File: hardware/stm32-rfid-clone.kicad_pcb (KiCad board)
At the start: 2 copper layers, 61 x 61 mm, 112 parts, among them J101 USB, M101 Mouting Hole, M102 Mouting Hole, M103 Mouting Hole, M104 Mouting Hole, P101 JTAG10, P102 BATTERY, P103 DEBUG, P104 READIND, P105 SPEAKER, P201 ANT, Q201 2N2222, Q202 2N2222, Q203 2N2907, U101 MOSFET-P, U102 STM32-48PIN, U103 AP6502, U104 MOSFET-N, U105 MIC2288, U201 TL084, X101 8MHz, X102 32.768kHz

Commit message: moved labels
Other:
- board text added: "+"
- board text added: "-"
- board text added: "ANT"
- board text added: "BAT"
- board text added: "DEBUG"
- board text added: "GND"
- board text added: "GRN"
- board text added: "JTAG"
- board text added: "LED"
- board text added: "PWR"
- board text added: "RED"
- board text added: "RF1"
- board text added: "RF2"
- board text added: "RF3"
- board text added: "RF4"
- board text added: "RX"
- board text added: "SPK"
- board text added: "THRESHOLD"
- board text added: "TX"
- board text added: "WRITEEN"

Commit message: update values
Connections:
- R115 pad 1: +3.3V -> +9V
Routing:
- net +3.3V: track 217.4 -> 201.4 mm
- net +9V: track 54.2 -> 62.3 mm, vias 2 -> 4
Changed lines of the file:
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@@
     (links 208)
     (no_connects 0)
-    (area 80.4478 75.353519 142.290001 148.628201)
+    (area 81.229999 78.689999 142.290001 139.750001)
     (thickness 1.6)
     (drawings 29)
-    (tracks 815)
+    (tracks 816)
     (zones 0)
     (modules 112)
@@
       (outputformat 1)
       (mirror false)
-      (drillshape 1)
+      (drillshape 0)
       (scaleselection 1)
       (outputdirectory ""))
@@
     (fp_line (start -1.7 1) (end -1.7 -1) (layer Cmts.User) (width 0.1))
     (pad 1 smd rect (at -0.95 0 270) (size 1 1.45) (layers F.Cu F.Paste F.Mask)
-      (net 1 +3.3V))
+      (net 2 +9V))
     (pad 2 smd rect (at 0.95 0 270) (size 1 1.45) (layers F.Cu F.Paste F.Mask)
       (net 50 "Net-(D105-Pad2)"))
@@
   (segment (start 87.2 102) (end 87.2 104.3) (width 0.254) (layer F.Cu) (net 1))
   (segment (start 85.96 100.76) (end 87.2 102) (width 0.254) (layer F.Cu) (net 1))
-  (segment (start 118 89.05) (end 118.55 89.05) (width 0.254) (layer F.Cu) (net 1))
-  (segment (start 118.55 89.05) (end 119.4 89.9) (width 0.254) (layer F.Cu) (net 1))
-  (segment (start 119.4 89.9) (end 119.4 91.7) (width 0.254) (layer F.Cu) (net 1))
-  (segment (start 119.4 91.7) (end 118.6 92.5) (width 0.254) (layer F.Cu) (net 1))
-  (segment (start 118.6 92.5) (end 115.7 92.5) (width 0.254) (layer F.Cu) (net 1))
-  (segment (start 115.7 92.5) (end 110 98.2) (width 0.254) (layer F.Cu) (net 1))
-  (segment (start 110 98.2) (end 110 98.55) (width 0.254) (layer F.Cu) (net 1))
   (segment (start 98.75 97.75) (end 98.75 96.65) (width 0.254) (layer F.Cu) (net 1))
   (segment (start 98.75 96.65) (end 97.55 95.45) (width 0.254) (layer F.Cu) (net 1))
@@
   (segment (start 115 126.45) (end 112.1 126.45) (width 0.4) (layer F.Cu) (net 1))
   (segment (start 112.1 126.45) (end 112 126.55) (width 0.4) (layer F.Cu) (net 1))
+  (segment (start 122.05 94.5) (end 122.05 94.05) (width 0.4) (layer F.Cu) (net 2))
+  (segment (start 118.55 89.05) (end 118 89.05) (width 0.4) (layer F.Cu) (net 2))
+  (segment (start 120.8 91.3) (end 118.55 89.05) (width 0.4) (layer F.Cu) (net 2))
+  (via (at 120.8 91.3) (size 0.889) (layers F.Cu B.Cu) (net 2))
+  (segment (start 122.8 93.3) (end 120.8 91.3) (width 0.4) (layer B.Cu) (net 2))
+  (via (at 122.8 93.3) (size 0.889) (layers F.Cu B.Cu) (net 2))
+  (segment (start 122.05 94.05) (end 122.8 93.3) (width 0.4) (layer F.Cu) (net 2))
   (segment (start 130.3 107.1) (end 129.4 106.2) (width 0.4) (layer B.Cu) (net 2))
   (via (at 124.1 100) (size 0.889) (layers F.Cu B.Cu) (net 2))
@@
   (segment (start 114.5 120.55) (end 112.95 120.55) (width 0.254) (layer F.Cu) (net 48))
   (segment (start 112.95 120.55) (end 112 119.6) (width 0.254) (layer F.Cu) (net 48))
-  (segment (start 114.3 81.28) (end 114.3 85.35) (width 0.254) (layer F.Cu) (net 49))
-  (segment (start 114.3 85.35) (end 114.45 85.5) (width 0.254) (layer F.Cu) (net 49))
-  (segment (start 115.15 90) (end 115.15 89.05) (width 0.254) (layer F.Cu) (net 49))
-  (segment (start 114.45 88.35) (end 114.45 85.5) (width 0.254) (layer F.Cu) (net 49))
-  (segment (start 115.15 89.05) (end 114.45 88.35) (width 0.254) (layer F.Cu) (net 49))
-  (segment (start 118 90.95) (end 117.85 90.95) (width 0.254) (layer F.Cu) (net 50))
-  (segment (start 112.65 91.8) (end 110.85 90) (width 0.254) (layer F.Cu) (net 50))
-  (segment (start 117 91.8) (end 112.65 91.8) (width 0.254) (layer F.Cu) (net 50))
-  (segment (start 117.85 90.95) (end 117 91.8) (width 0.254) (layer F.Cu) (net 50))
-  (segment (start 111.76 81.28) (end 111.76 81.76) (width 0.254) (layer F.Cu) (net 50))
-  (segment (start 113 87.85) (end 110.85 90) (width 0.254) (layer F.Cu) (net 50))
-  (segment (start 113 83) (end 113 87.85) (width 0.254) (layer F.Cu) (net 50))
-  (segment (start 111.76 81.76) (end 113 83) (width 0.254) (layer F.Cu) (net 50))
+  (segment (start 114.3 81.28) (end 114.3 85.35) (width 0.4) (layer F.Cu) (net 49))
+  (segment (start 114.3 85.35) (end 114.45 85.5) (width 0.4) (layer F.Cu) (net 49))
+  (segment (start 115.15 90) (end 115.15 89.05) (width 0.4) (layer F.Cu) (net 49))
+  (segment (start 115.15 89.05) (end 114.45 88.35) (width 0.4) (layer F.Cu) (net 49))
+  (segment (start 114.45 88.35) (end 114.45 85.5) (width 0.4) (layer F.Cu) (net 49))
+  (segment (start 118 90.95) (end 117.85 90.95) (width 0.4) (layer F.Cu) (net 50))
+  (segment (start 117.85 90.95) (end 117 91.8) (width 0.4) (layer F.Cu) (net 50))
+  (segment (start 117 91.8) (end 112.65 91.8) (width 0.4) (layer F.Cu) (net 50))
+  (segment (start 112.65 91.8) (end 110.85 90) (width 0.4) (layer F.Cu) (net 50))
+  (segment (start 111.76 81.28) (end 111.76 81.76) (width 0.4) (layer F.Cu) (net 50))
+  (segment (start 111.76 81.76) (end 113 83) (width 0.4) (layer F.Cu) (net 50))
+  (segment (start 113 83) (end 113 87.85) (width 0.4) (layer F.Cu) (net 50))
+  (segment (start 113 87.85) (end 110.85 90) (width 0.4) (layer F.Cu) (net 50))
   (segment (start 132 122.5) (end 124.65 122.5) (width 0.4) (layer F.Cu) (net 51))
   (segment (start 124.65 122.5) (end 123.65 121.5) (width 0.4) (layer F.Cu) (net 51))
@@
   (segment (start 117.45 96.55) (end 115 96.55) (width 0.254) (layer F.Cu) (net 62))
   (segment (start 115 96.55) (end 114.5 97.05) (width 0.254) (layer F.Cu) (net 62))
-  (segment (start 122.05 96.95) (end 122.05 96.75) (width 0.4) (layer F.Cu) (net 63))
-  (segment (start 124.55 92.9) (end 126 91.45) (width 0.4) (layer F.Cu) (net 63))
-  (segment (start 121.7 92.9) (end 124.55 92.9) (width 0.4) (layer F.Cu) (net 63))
-  (segment (start 120.9 93.7) (end 121.7 92.9) (width 0.4) (layer F.Cu) (net 63))
-  (segment (start 120.9 95.6) (end 120.9 93.7) (width 0.4) (layer F.Cu) (net 63))
+  (segment (start 120.9 93.7) (end 120.9 93.6) (width 0.4) (layer F.Cu) (net 63))
   (segment (start 122.05 96.75) (end 120.9 95.6) (width 0.4) (layer F.Cu) (net 63))
+  (segment (start 120.9 95.6) (end 120.9 93.7) (width 0.4) (layer F.Cu) (net 63))
+  (segment (start 122.05 96.95) (end 122.05 96.75) (width 0.4) (layer F.Cu) (net 63))
+  (segment (start 125.05 92.4) (end 126 91.45) (width 0.4) (layer F.Cu) (net 63))
+  (segment (start 122.1 92.4) (end 125.05 92.4) (width 0.4) (layer F.Cu) (net 63))
+  (segment (start 120.9 93.6) (end 122.1 92.4) (width 0.4) (layer F.Cu) (net 63))
   (segment (start 120.8 96.5) (end 120.1 95.8) (width 0.4) (layer F.Cu) (net 64))
   (segment (start 123.5 91.45) (end 122.25 91.45) (width 0.4) (layer F.Cu) (net 64))

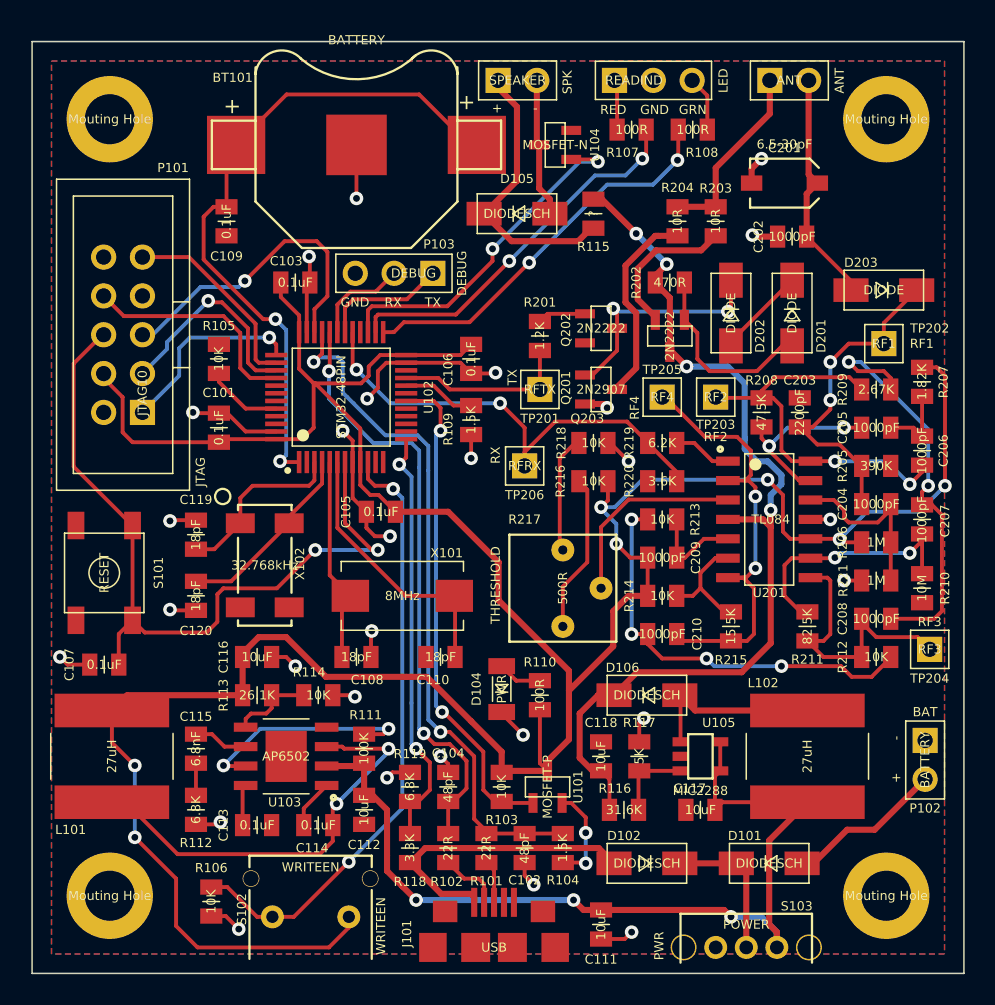
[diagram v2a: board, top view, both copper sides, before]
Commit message: update schematic
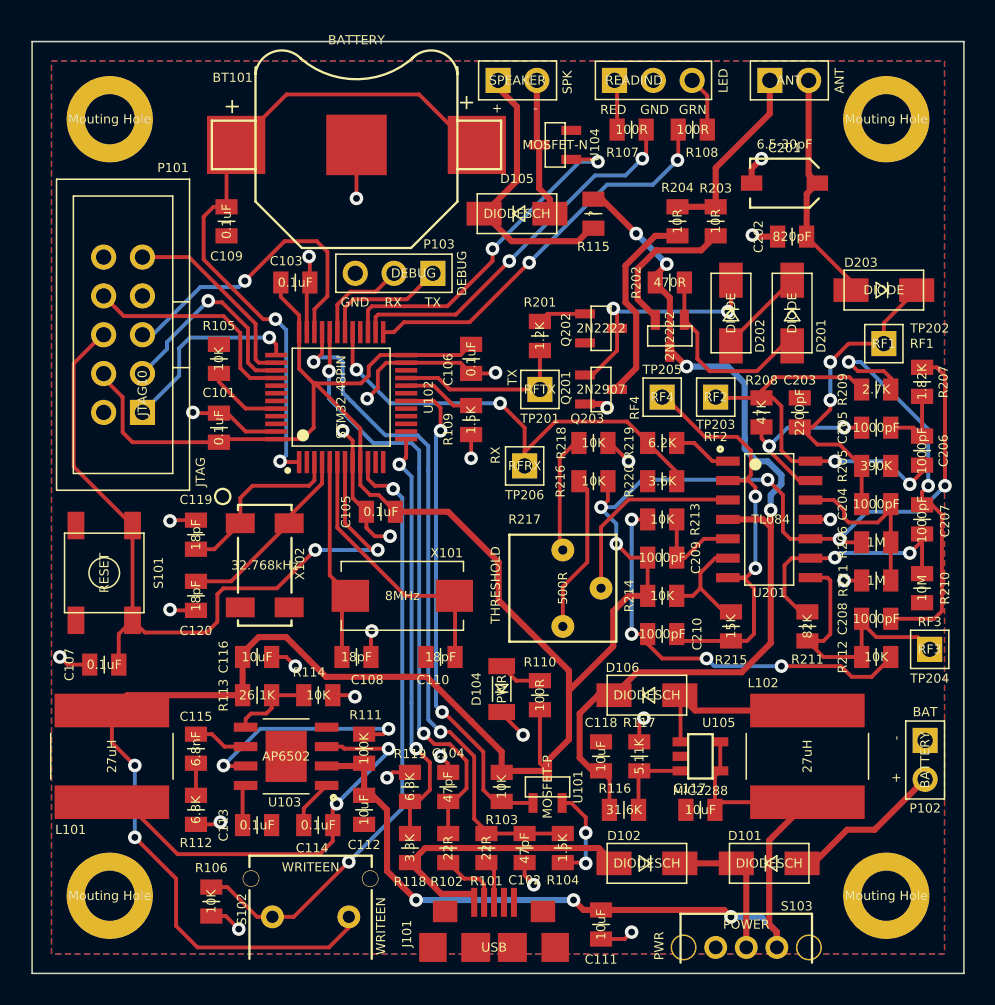
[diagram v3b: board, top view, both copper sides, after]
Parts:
- C102, C104: value 48pF -> 47pF
- C202: value 1000pF -> 820pF
- R117: value 5K -> 5.11K
- R208: value 47.5K -> 47K
- R209: value 2.67K -> 2.7K
- R211: value 82.5K -> 82K
- R215: value 15.5K -> 15K
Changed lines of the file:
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@@
   )
   (setup
-    (last_trace_width 0.4)
+    (last_trace_width 0.254)
     (user_trace_width 0.4)
     (trace_clearance 0.2032)
@@
       (effects (font (size 0.6 0.6) (thickness 0.1)))
     )
-    (fp_text value 48pF (at 0 0 270) (layer F.SilkS)
+    (fp_text value 47pF (at 0 0 270) (layer F.SilkS)
       (effects (font (size 0.6 0.6) (thickness 0.1)))
     )
@@
       (effects (font (size 0.6 0.6) (thickness 0.1)))
     )
-    (fp_text value 48pF (at 0 0 90) (layer F.SilkS)
+    (fp_text value 47pF (at 0 0 90) (layer F.SilkS)
       (effects (font (size 0.6 0.6) (thickness 0.1)))
     )
@@
       (effects (font (size 0.6 0.6) (thickness 0.1)))
     )
-    (fp_text value 1000pF (at 0 0 180) (layer F.SilkS)
+    (fp_text value 820pF (at 0 0 180) (layer F.SilkS)
       (effects (font (size 0.6 0.6) (thickness 0.1)))
     )
@@
       (effects (font (size 0.6 0.6) (thickness 0.1)))
     )
-    (fp_text value 5K (at 0 0 90) (layer F.SilkS)
+    (fp_text value 5.11K (at 0 0 90) (layer F.SilkS)
       (effects (font (size 0.6 0.6) (thickness 0.1)))
     )
@@
       (effects (font (size 0.6 0.6) (thickness 0.1)))
     )
-    (fp_text value 47.5K (at 0 0 90) (layer F.SilkS)
+    (fp_text value 47K (at 0 0 90) (layer F.SilkS)
       (effects (font (size 0.6 0.6) (thickness 0.1)))
     )
@@
       (effects (font (size 0.6 0.6) (thickness 0.1)))
     )
-    (fp_text value 2.67K (at 0 0) (layer F.SilkS)
+    (fp_text value 2.7K (at 0 0) (layer F.SilkS)
       (effects (font (size 0.6 0.6) (thickness 0.1)))
     )
@@
       (effects (font (size 0.6 0.6) (thickness 0.1)))
     )
-    (fp_text value 82.5K (at 0 0 270) (layer F.SilkS)
+    (fp_text value 82K (at 0 0 270) (layer F.SilkS)
       (effects (font (size 0.6 0.6) (thickness 0.1)))
     )
@@
       (effects (font (size 0.6 0.6) (thickness 0.1)))
     )
-    (fp_text value 15.5K (at 0 0 90) (layer F.SilkS)
-      (effects (font (size 0.6 0.6) (thickness 0.1)))
-    )
+    (fp_text value 15K (at 0 0 90) (layer F.SilkS)
+      (effects (font (size 0.6 0.6) (thickness 0.1)))
+    )

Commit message: 2014-01-14
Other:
- board text added: "ANT ADJ"
- board text added: "RESET"
- board text added: "STM32 RFID Clone Joe Ferner 2014-01-14"
- board text added: "https://github.com/joeferner/stm32-rfid-clone"
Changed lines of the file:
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@@
     (links 208)
     (no_connects 0)
-    (area 81.229999 78.689999 142.290001 139.750001)
+    (area 81.229999 75.353519 142.410343 148.628201)
     (thickness 1.6)
-    (drawings 29)
+    (drawings 33)
     (tracks 816)
     (zones 0)
@@
     (visible_elements FFFEFF7F)
     (pcbplotparams
-      (layerselection 3178497)
+      (layerselection 284196865)
       (usegerberextensions true)
-      (excludeedgelayer true)
+      (excludeedgelayer false)
       (linewidth 0.150000)
       (plotframeref false)
@@
       (psa4output false)
       (plotreference true)
-      (plotvalue true)
+      (plotvalue false)
       (plotothertext true)
       (plotinvisibletext false)
@@
       (drillshape 0)
       (scaleselection 1)
-      (outputdirectory ""))
+      (outputdirectory /home/jferner/dev/stm32-rfid-clone/hardware/2014-01-14/))
   )
   (net 0 "")
@@
   (module stm32:DIOM5226X220N (layer F.Cu)
     (at 113 90 180)
-    (fp_text reference D105 (at 0 2.286 180) (layer F.SilkS)
+    (fp_text reference D105 (at 0 1.8 180) (layer F.SilkS)
       (effects (font (size 0.6 0.6) (thickness 0.1)))
     )
@@
       (net 33 "Net-(C120-Pad1)"))
   )
+  (gr_text "ANT\nADJ" (at 134.7 88) (layer F.SilkS)
+    (effects (font (size 0.6 0.6) (thickness 0.1)))
+  )
+  (gr_text RESET (at 86 108.8) (layer F.SilkS)
+    (effects (font (size 0.6 0.6) (thickness 0.1)))
+  )
+  (gr_text https://github.com/joeferner/stm32-rfid-clone (at 111.2 128.8) (layer B.SilkS)
+    (effects (font (size 1 1) (thickness 0.2)) (justify mirror))
+  )
+  (gr_text "STM32 RFID Clone\nJoe Ferner\n2014-01-14" (at 110.1 83.6) (layer B.SilkS)
+    (effects (font (size 1.5 1.5) (thickness 0.3)) (justify left mirror))
+  )
   (gr_text JTAG (at 92.3 106.9 90) (layer F.SilkS)

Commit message: update to values
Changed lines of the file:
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@@
   (module stm32:SOT95P237X112_123-3N (layer F.Cu)
     (at 118.5 97.5)
-    (fp_text reference Q201 (at -2.3 3.9 90) (layer F.SilkS)
+    (fp_text reference Q201 (at -2.3 0.1 90) (layer F.SilkS)
       (effects (font (size 0.6 0.6) (thickness 0.1)))
     )
@@
   (module stm32:SOT95P237X112_123-3N (layer F.Cu)
     (at 123 98 270)
-    (fp_text reference Q202 (at -0.4 6.8 270) (layer F.SilkS)
+    (fp_text reference Q202 (at 0.1 2 270) (layer F.SilkS)
       (effects (font (size 0.6 0.6) (thickness 0.1)))
     )
@@
   (module stm32:SOT95P237X112_123-3N (layer F.Cu)
     (at 118.5 101.5)
-    (fp_text reference Q203 (at -0.9 1.9) (layer F.SilkS)
+    (fp_text reference Q203 (at -2.3 -0.1 90) (layer F.SilkS)
       (effects (font (size 0.6 0.6) (thickness 0.1)))
     )
